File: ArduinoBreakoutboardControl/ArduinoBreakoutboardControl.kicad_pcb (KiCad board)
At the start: 2 copper layers, 39.4 x 80.9 mm, 143 parts, among them M1 Conn_01x06_Male

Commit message: Added ground fill, fixed edge cuts, fixed 90 degree angles,
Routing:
- net GND: track 194.6 -> 4.49 mm
- net Net-(A1-Pad30): track 124.3 -> 115.4 mm
- added copper zone on B.Cu, net GND
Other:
- board size 39.4 x 80.9 mm -> 39.4 x 82.7 mm
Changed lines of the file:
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@@
   (general
     (thickness 1.6)
-    (drawings 33)
-    (tracks 178)
+    (drawings 41)
+    (tracks 147)
     (zones 0)
     (modules 143)
@@
   (layers
     (0 F.Cu signal)
-    (31 B.Cu signal)
-    (32 B.Adhes user)
-    (33 F.Adhes user)
-    (34 B.Paste user)
-    (35 F.Paste user)
+    (31 B.Cu signal hide)
+    (32 B.Adhes user hide)
+    (33 F.Adhes user hide)
+    (34 B.Paste user hide)
+    (35 F.Paste user hide)
     (36 B.SilkS user)
-    (37 F.SilkS user)
+    (37 F.SilkS user hide)
     (38 B.Mask user)
     (39 F.Mask user)
@@
     )
   )
-  (gr_line (start 132.334 41.91) (end 132.334 122.809) (layer Edge.Cuts) (width 0.1))
-  (gr_line (start 171.704 41.91) (end 132.334 41.91) (layer Edge.Cuts) (width 0.1))
-  (gr_line (start 171.704 114.554) (end 171.704 41.91) (layer Edge.Cuts) (width 0.1))
+  (gr_arc (start 151.892 82.296) (end 151.13 82.296) (angle -180) (layer B.SilkS) (width 0.12))
+  (gr_line (start 151.13 82.296) (end 152.654 82.296) (layer B.SilkS) (width 0.12))
+  (gr_circle (center 155.736094 80.518) (end 157.514094 79.756) (layer B.SilkS) (width 0.12))
+  (gr_circle (center 155.736094 80.518) (end 157.4165 80.264) (layer B.SilkS) (width 0.12))
+  (gr_circle (center 155.736094 80.518) (end 157.1625 79.502) (layer B.SilkS) (width 0.12))
+  (gr_circle (center 148.179594 80.518) (end 149.606 79.502) (layer B.SilkS) (width 0.12))
+  (gr_circle (center 148.179594 80.518) (end 149.86 80.264) (layer B.SilkS) (width 0.12))
+  (gr_circle (center 148.179594 80.518) (end 149.957594 79.756) (layer B.SilkS) (width 0.12))
+  (gr_line (start 132.334 40.132) (end 132.334 122.809) (layer Edge.Cuts) (width 0.1))
+  (gr_line (start 171.704 40.132) (end 132.334 40.132) (layer Edge.Cuts) (width 0.1))
+  (gr_line (start 171.704 114.554) (end 171.704 40.132) (layer Edge.Cuts) (width 0.1))
   (gr_line (start 163.449 122.809) (end 171.704 114.554) (layer Edge.Cuts) (width 0.1))
   (gr_line (start 132.334 122.809) (end 163.449 122.809) (layer Edge.Cuts) (width 0.1))
@@
   (segment (start 137.16 109.655) (end 138.63 109.655) (width 0.4572) (layer F.Cu) (net 2))
   (segment (start 140.97 107.315) (end 144.145 107.315) (width 1.524) (layer F.Cu) (net 2))
-  (segment (start 141.6422 118.11) (end 140.335 118.11) (width 0.4572) (layer F.Cu) (net 3))
-  (segment (start 145.4522 114.3) (end 141.6422 118.11) (width 0.4572) (layer F.Cu) (net 3))
-  (segment (start 151.765 114.3) (end 145.4522 114.3) (width 0.4572) (layer F.Cu) (net 3))
-  (segment (start 151.765 71.755) (end 151.765 114.3) (width 0.4572) (layer F.Cu) (net 3))
-  (segment (start 159.385 71.755) (end 151.765 71.755) (width 0.4572) (layer F.Cu) (net 3))
   (segment (start 163.973492 71.755) (end 162.56 71.755) (width 0.4572) (layer F.Cu) (net 3))
   (segment (start 167.798091 67.930401) (end 163.973492 71.755) (width 0.4572) (layer F.Cu) (net 3))
@@
   (segment (start 167.798091 45.034515) (end 167.798091 67.930401) (width 0.4572) (layer F.Cu) (net 3))
   (segment (start 159.385 71.755) (end 162.56 71.755) (width 1.524) (layer F.Cu) (net 3))
+  (segment (start 158.585001 72.554999) (end 159.385 71.755) (width 0.4572) (layer F.Cu) (net 3))
+  (segment (start 146.030811 85.109189) (end 158.585001 72.554999) (width 0.4572) (layer F.Cu) (net 3))
+  (segment (start 146.030811 110.956989) (end 146.030811 85.109189) (width 0.4572) (layer F.Cu) (net 3))
+  (segment (start 140.335 116.6528) (end 146.030811 110.956989) (width 0.4572) (layer F.Cu) (net 3))
+  (segment (start 140.335 118.11) (end 140.335 116.6528) (width 0.4572) (layer F.Cu) (net 3))
   (segment (start 140.97 104.775) (end 144.145 104.775) (width 1.524) (layer F.Cu) (net 4))
   (segment (start 139.970511 103.234489) (end 140.97 102.235) (width 0.4572) (layer F.Cu) (net 5))
@@
   (segment (start 140.97 81.915) (end 144.145 81.915) (width 1.524) (layer F.Cu) (net 21))
   (segment (start 159.385 97.155) (end 162.56 97.155) (width 1.524) (layer F.Cu) (net 22))
-  (segment (start 139.556508 79.375) (end 140.97 79.375) (width 0.4572) (layer B.Cu) (net 23))
-  (segment (start 137.806773 79.375) (end 139.556508 79.375) (width 0.4572) (layer B.Cu) (net 23))
-  (segment (start 135.75639 77.324617) (end 137.806773 79.375) (width 0.4572) (layer B.Cu) (net 23))
   (segment (start 137.16 71.795) (end 137.035 71.795) (width 0.4572) (layer B.Cu) (net 23))
-  (segment (start 154.305 79.375) (end 159.385 74.295) (width 0.4572) (layer B.Cu) (net 23))
-  (segment (start 144.145 79.375) (end 154.305 79.375) (width 0.4572) (layer B.Cu) (net 23))
   (segment (start 166.965 78.7) (end 167.64 78.7) (width 0.4572) (layer B.Cu) (net 23))
-  (segment (start 162.56 74.295) (end 166.965 78.7) (width 0.4572) (layer B.Cu) (net 23))
-  (segment (start 156.576667 115.411909) (end 140.533091 115.411909) (width 0.4572) (layer B.Cu) (net 23))
-  (segment (start 169.04361 102.944966) (end 156.576667 115.411909) (width 0.4572) (layer B.Cu) (net 23))
-  (segment (start 140.533091 115.411909) (end 138.740553 117.204447) (width 0.4572) (layer B.Cu) (net 23))
-  (segment (start 169.04361 79.97861) (end 169.04361 102.944966) (width 0.4572) (layer B.Cu) (net 23))
-  (segment (start 167.765 78.7) (end 169.04361 79.97861) (width 0.4572) (layer B.Cu) (net 23))
   (segment (start 167.64 78.7) (end 167.765 78.7) (width 0.4572) (layer B.Cu) (net 23))
-  (segment (start 138.740553 87.140553) (end 137.285 85.685) (width 0.4572) (layer B.Cu) (net 23))
-  (segment (start 137.835 118.11) (end 138.740553 117.204447) (width 0.4572) (layer B.Cu) (net 23))
-  (segment (start 139.970511 80.374489) (end 140.97 79.375) (width 0.4572) (layer B.Cu) (net 23))
-  (segment (start 139.541909 80.803091) (end 139.970511 80.374489) (width 0.4572) (layer B.Cu) (net 23))
-  (segment (start 139.541909 83.428091) (end 139.541909 80.803091) (width 0.4572) (layer B.Cu) (net 23))
-  (segment (start 137.285 85.685) (end 139.541909 83.428091) (width 0.4572) (layer B.Cu) (net 23))
   (segment (start 137.16 85.685) (end 137.285 85.685) (width 0.4572) (layer B.Cu) (net 23))
-  (segment (start 138.43 63.5) (end 138.43 60.96) (width 1.524) (layer B.Cu) (net 23))
-  (segment (start 138.43 58.42) (end 138.43 60.96) (width 1.524) (layer B.Cu) (net 23))
-  (segment (start 138.43 55.88) (end 138.43 58.42) (width 1.524) (layer B.Cu) (net 23))
-  (segment (start 138.43 53.34) (end 138.43 55.88) (width 1.524) (layer B.Cu) (net 23))
-  (segment (start 138.43 50.8) (end 138.43 53.34) (width 1.524) (layer B.Cu) (net 23))
-  (segment (start 137.035 71.795) (end 135.75639 73.07361) (width 0.4572) (layer B.Cu) (net 23))
-  (segment (start 135.75639 73.07361) (end 135.75639 77.324617) (width 0.4572) (layer B.Cu) (net 23))
-  (segment (start 135.7278 70.4878) (end 137.035 71.795) (width 0.4572) (layer B.Cu) (net 23))
-  (segment (start 137.795 45.085) (end 135.7278 47.1522) (width 0.4572) (layer B.Cu) (net 23))
-  (segment (start 135.7278 47.1522) (end 135.7278 70.4878) (width 0.4572) (layer B.Cu) (net 23))
   (segment (start 138.43 45.72) (end 137.795 45.085) (width 0.4572) (layer B.Cu) (net 23))
-  (segment (start 138.43 50.8) (end 138.43 45.72) (width 0.4572) (layer B.Cu) (net 23))
-  (segment (start 140.97 79.375) (end 144.145 79.375) (width 1.524) (layer B.Cu) (net 23))
-  (segment (start 159.385 74.295) (end 162.56 74.295) (width 1.524) (layer B.Cu) (net 23))
-  (segment (start 138.740553 117.204447) (end 138.740553 87.140553) (width 0.4572) (layer B.Cu) (net 23))
   (segment (start 158.115 116.84) (end 158.115 119.38) (width 0.4572) (layer B.Cu) (net 23))
   (segment (start 159.385 99.695) (end 162.56 99.695) (width 1.524) (layer F.Cu) (net 24))
@@
   (segment (start 160.655 116.84) (end 160.655 115.426508) (width 0.4572) (layer F.Cu) (net 28))
   (segment (start 140.97 71.755) (end 144.145 71.755) (width 1.524) (layer F.Cu) (net 29))
+  (zone (net 23) (net_name GND) (layer B.Cu) (hatch edge 0.508)
+    (connect_pads (clearance 0.508))
+    (min_thickness 0.254)
+    (fill yes (arc_segments 32) (thermal_gap 0.508) (thermal_bridge_width 0.508))
+    (polygon
+      (pts
+        (xy 132.842 121.92) (xy 163.322 121.92) (xy 170.942 114.3) (xy 170.942 42.672) (xy 133.35 42.672)
+      )
+    )
+  )
 )

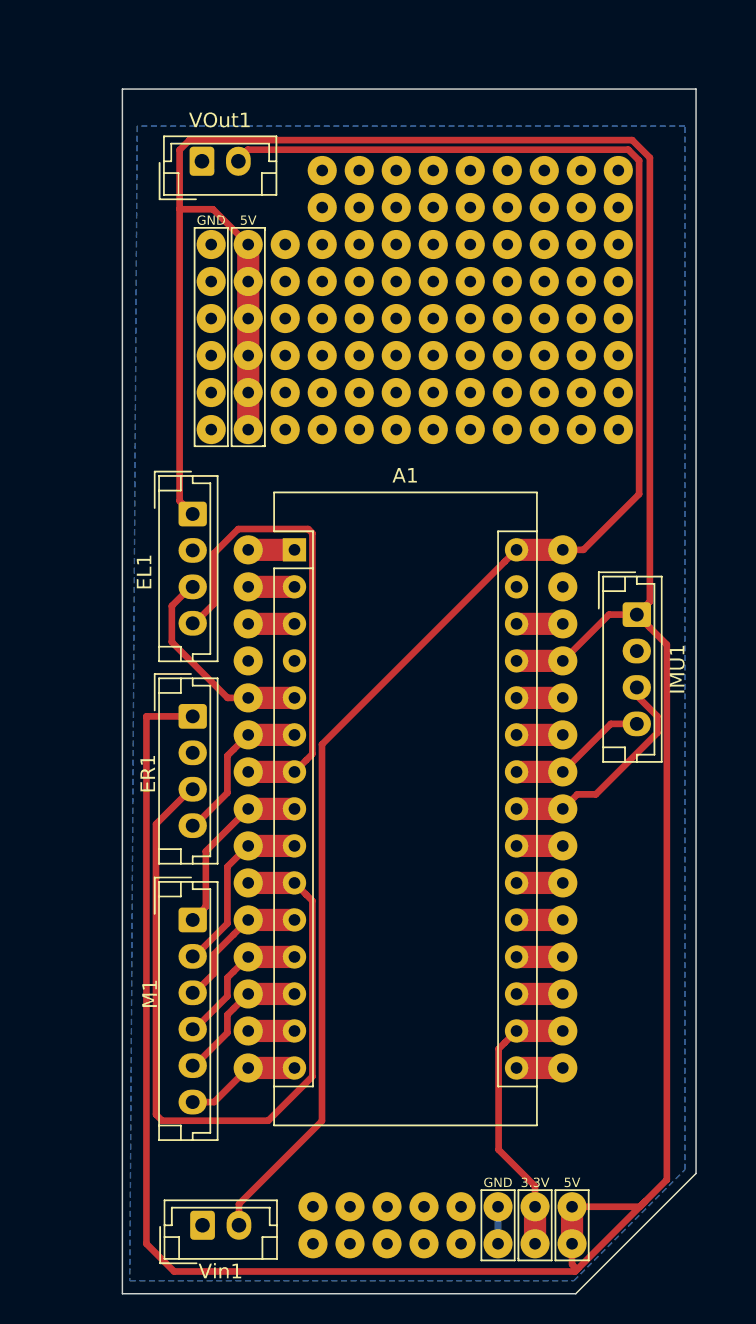
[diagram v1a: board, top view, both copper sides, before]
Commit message: fixed more 90 degree angles, Added drill holes
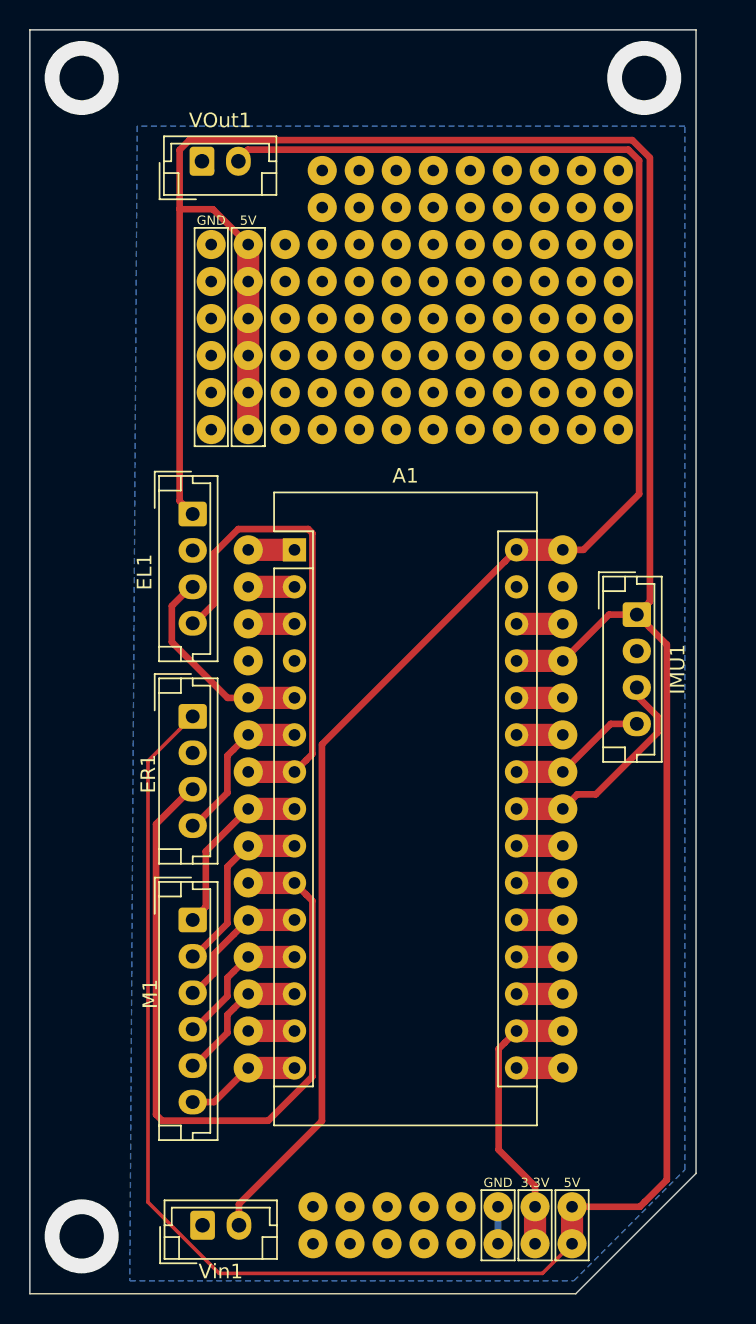
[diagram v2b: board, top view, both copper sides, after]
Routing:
- net Net-(A1-Pad27): track 245.9 -> 234.2 mm
- net (no net): vias 0 -> 3
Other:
- board size 39.4 x 82.7 mm -> 45.7 x 86.7 mm

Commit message: Completly rerouted traces across the board, added more space between the traces, added more description for the pads
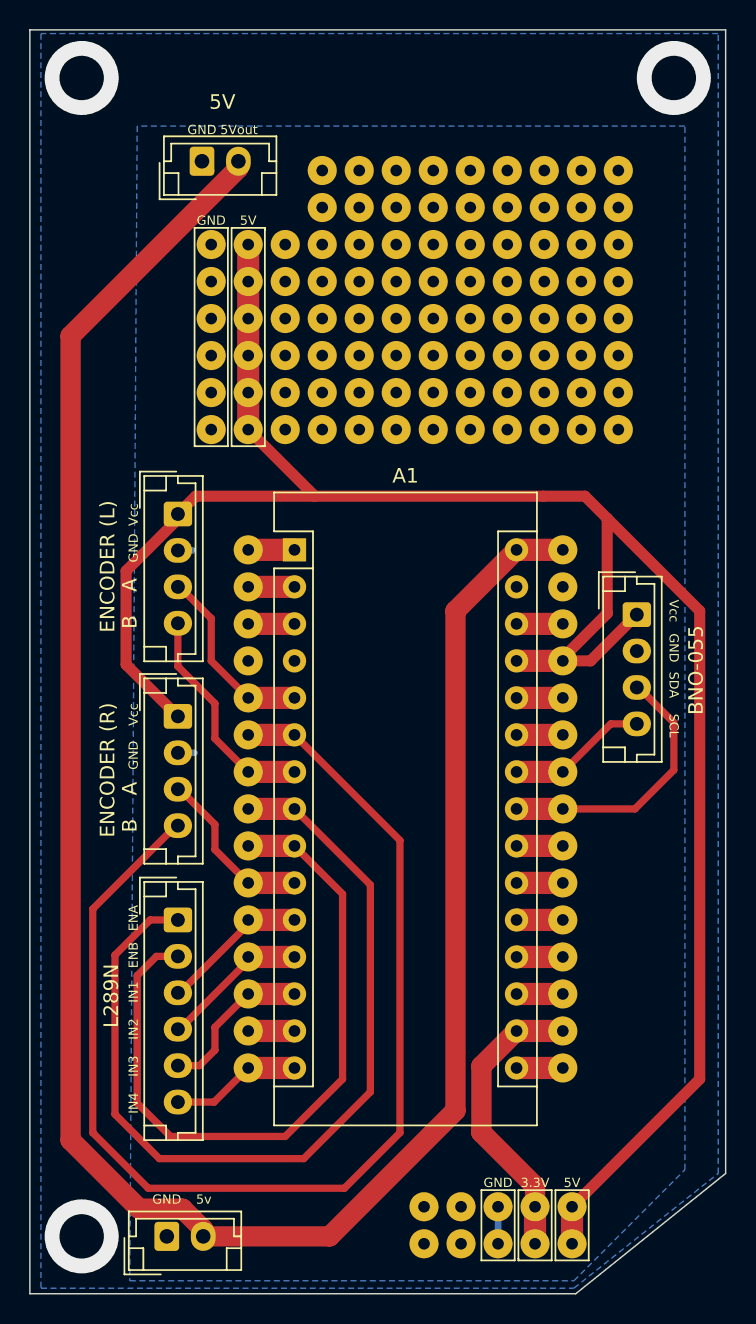
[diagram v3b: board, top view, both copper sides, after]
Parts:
- removed the PAD at (148.0, 116.8)
- removed the PAD at (145.4, 116.8)
- removed the PAD at (150.5, 116.8)
- removed the PAD at (150.5, 119.4)
- removed the PAD at (145.4, 119.4)
- removed the PAD at (148.0, 119.4)
- ENCODER (L): renamed from EL1
- ENCODER (R): renamed from ER1
- moved 5v 2.57 mm to (135.4, 118.9)
- moved ENCODER (L) 1.02 mm to (136.1, 69.3)
- moved ENCODER (R) 1.02 mm to (136.1, 83.2)
- moved L289N 1.02 mm to (136.1, 97.2)
- renumbered VOut1 to 5V, Vin1 to 5v, IMU1 to BNO-055, M1 to L289N
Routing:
- net Net-(A1-Pad27): track 234.2 -> 143.3 mm
- net Net-(A1-Pad6): track 11.2 -> 81.4 mm
- net Net-(A1-Pad8): track 12.4 -> 61.7 mm
- net Net-(A1-Pad10): track 52.6 -> 11.7 mm
- net Net-(A1-Pad9): track 12.4 -> 49.8 mm
- net Net-(A1-Pad30): track 115.4 -> 148.7 mm
- net Net-(A1-Pad7): track 33.1 -> 15.4 mm
- net Net-(A1-Pad23): track 15.5 -> 19.4 mm
- net Net-(A1-Pad5): track 14.6 -> 12.9 mm
- net Net-(A1-Pad13): track 9.75 -> 11.0 mm
- net Net-(A1-Pad15): track 7.95 -> 8.97 mm
- net Net-(A1-Pad17): track 19.3 -> 20.3 mm
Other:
- board size 45.7 x 86.7 mm -> 47.8 x 86.7 mm
- rule pad_to_mask_clearance: 0.051 -> 0.0508
- rule solder_mask_min_width: 0.25 -> 0.1
- board text added: "5Vout"
- board text added: "A"
- board text added: "B"
- board text added: "ENA"
- board text added: "ENB"
- board text added: "IN1"
- board text added: "IN2"
- board text added: "IN3"
- board text added: "IN4"
- board text added: "SCL"
- board text added: "SDA"
- board text added: "Vcc"

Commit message: made the traces on arduino to buffer pins thinner, gave more space in between the traces, and added more data sheets to git
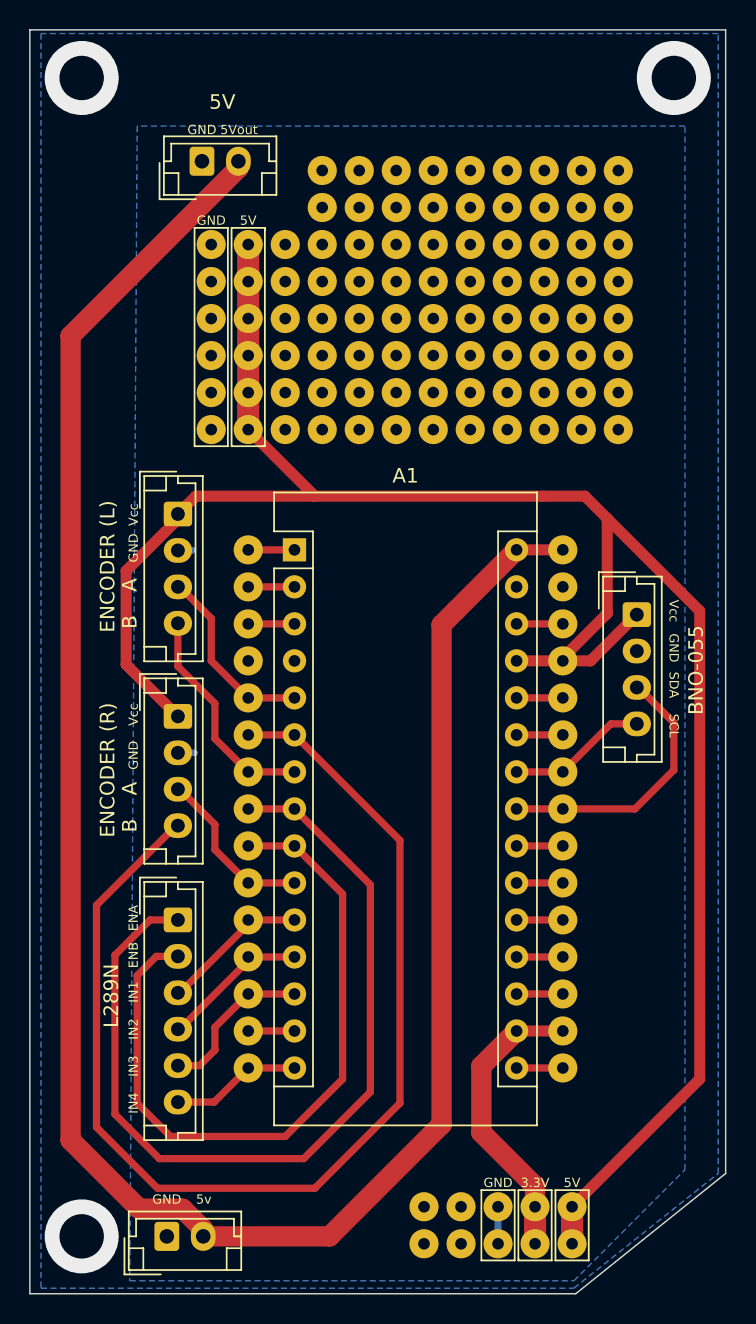
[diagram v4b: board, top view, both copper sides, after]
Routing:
- net Net-(A1-Pad6): track 81.4 -> 79.6 mm

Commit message: updated sensor board worked on by olivia ??? changes made
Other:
- board text added: "Designer:Jorge Exinia"
- board text added: "V 1.0"
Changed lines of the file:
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@@
   (general
     (thickness 1.6)
-    (drawings 90)
+    (drawings 92)
     (tracks 142)
     (zones 0)
@@
     (32 B.Adhes user hide)
     (33 F.Adhes user hide)
-    (34 B.Paste user)
-    (35 F.Paste user)
-    (36 B.SilkS user hide)
-    (37 F.SilkS user)
+    (34 B.Paste user hide)
+    (35 F.Paste user hide)
+    (36 B.SilkS user)
+    (37 F.SilkS user hide)
     (38 B.Mask user)
     (39 F.Mask user)
@@
     (44 Edge.Cuts user)
     (45 Margin user hide)
-    (46 B.CrtYd user hide)
+    (46 B.CrtYd user)
     (47 F.CrtYd user)
-    (48 B.Fab user hide)
-    (49 F.Fab user hide)
+    (48 B.Fab user)
+    (49 F.Fab user)
   )
   (setup
-    (last_trace_width 0.762)
+    (last_trace_width 0.25)
     (user_trace_width 0.5)
     (user_trace_width 0.762)
@@
     )
   )
+  (gr_text "V 1.0" (at 172.847 106.299 90) (layer B.SilkS)
+    (effects (font (size 1 1) (thickness 0.15)) (justify mirror))
+  )
+  (gr_text "Designer:Jorge Exinia" (at 171.069 106.426 90) (layer B.SilkS)
+    (effects (font (size 1 1) (thickness 0.15)) (justify mirror))
+  )
   (gr_text GND (at 137.795 42.926) (layer F.SilkS)
